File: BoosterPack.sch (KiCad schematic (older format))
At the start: 0 parts

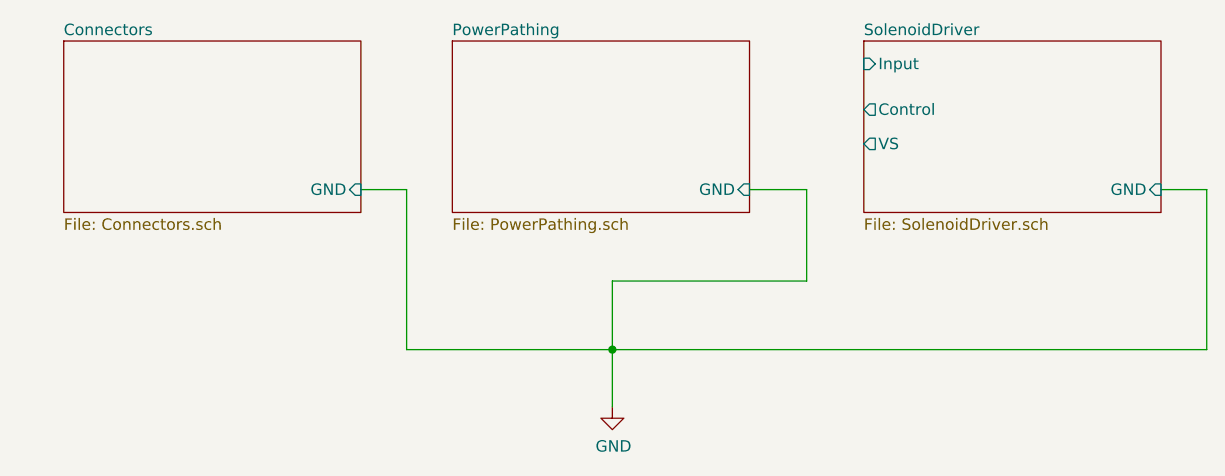
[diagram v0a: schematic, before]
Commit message: Schematic Updates
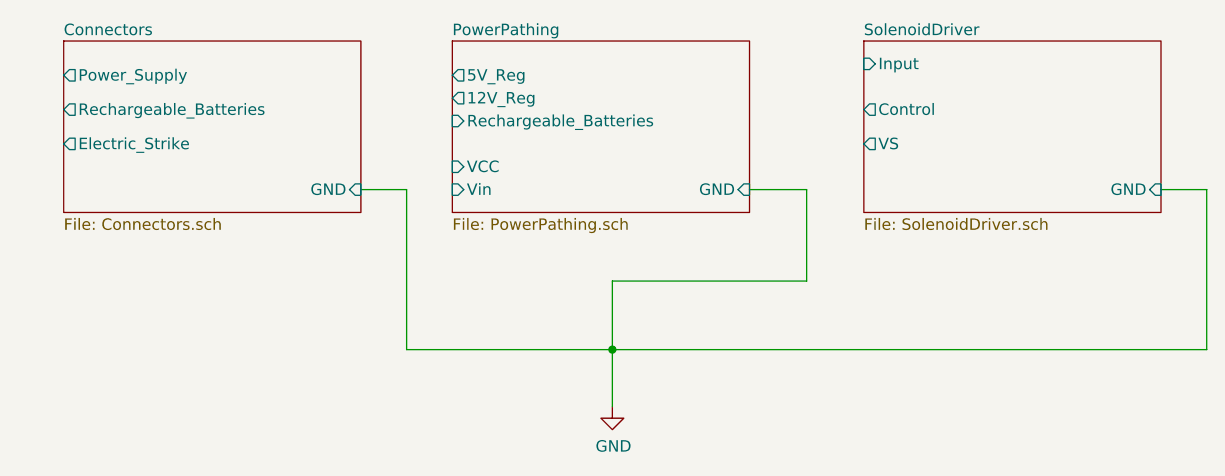
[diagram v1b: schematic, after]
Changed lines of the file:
@@
 F1 "PowerPathing.sch" 50
 F2 "GND" I R 4850 3300 50
+F3 "Vin" I L 3550 3300 50
+F4 "VCC" I L 3550 3200 50
+F5 "Rechargeable_Batteries" I L 3550 3000 50
+F6 "5V_Reg" O L 3550 2800 50
+F7 "12V_Reg" O L 3550 2900 50
 $EndSheet
 $Sheet
@@
 F1 "Connectors.sch" 50
 F2 "GND" I R 3150 3300 50
+F3 "Power_Supply" O L 1850 2800 50
+F4 "Rechargeable_Batteries" O L 1850 2950 50
+F5 "Electric_Strike" O L 1850 3100 50
 $EndSheet
 $Comp

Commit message: Schematic Updates, still need component values for driver circuit and keypad connector EDA
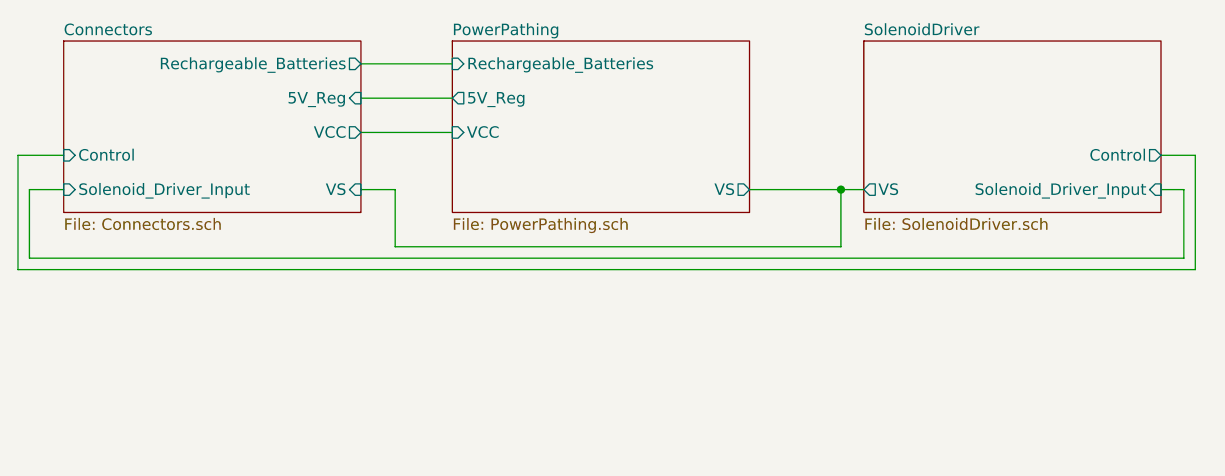
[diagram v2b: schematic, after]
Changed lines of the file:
@@
 F0 "PowerPathing" 50
 F1 "PowerPathing.sch" 50
-F2 "GND" I R 4850 3300 50
-F3 "Vin" I L 3550 3300 50
-F4 "VCC" I L 3550 3200 50
-F5 "Rechargeable_Batteries" I L 3550 3000 50
-F6 "5V_Reg" O L 3550 2800 50
-F7 "12V_Reg" O L 3550 2900 50
+F2 "VCC" I L 3550 3050 50
+F3 "Rechargeable_Batteries" I L 3550 2750 50
+F4 "5V_Reg" O L 3550 2900 50
+F5 "VS" O R 4850 3300 50
+$EndSheet
+$Sheet
+S 1850 2650 1300 750
+U 61536750
+F0 "Connectors" 50
+F1 "Connectors.sch" 50
+F2 "Rechargeable_Batteries" O R 3150 2750 50
+F3 "5V_Reg" I R 3150 2900 50
+F4 "Solenoid_Driver_Input" I L 1850 3300 50
+F5 "VCC" O R 3150 3050 50
+F6 "VS" I R 3150 3300 50
+F7 "Control" I L 1850 3150 50
 $EndSheet
 $Sheet
@@
 F0 "SolenoidDriver" 50
 F1 "SolenoidDriver.sch" 50
-F2 "GND" I R 6650 3300 50
-F3 "Control" O L 5350 2950 50
-F4 "VS" O L 5350 3100 50
-F5 "Input" I L 5350 2750 50
+F2 "Control" O R 6650 3150 50
+F3 "VS" O L 5350 3300 50
+F4 "Solenoid_Driver_Input" I R 6650 3300 50
 $EndSheet
-$Sheet
-S 1850 2650 1300 750
-U 61536750
-F0 "Connectors" 50
-F1 "Connectors.sch" 50
-F2 "GND" I R 3150 3300 50
-F3 "Power_Supply" O L 1850 2800 50
-F4 "Rechargeable_Batteries" O L 1850 2950 50
-F5 "Electric_Strike" O L 1850 3100 50
-$EndSheet
-$Comp
-L power:GND #PWR?
-U 1 1 615662EA
-P 4250 4250
-F 0 "#PWR?" H 4250 4000 50  0001 C CNN
-F 1 "GND" H 4255 4077 50  0000 C CNN
-F 2 "" H 4250 4250 50  0001 C CNN
-F 3 "" H 4250 4250 50  0001 C CNN
-	1    4250 4250
-	1    0    0    -1
-$EndComp
 Wire Wire Line
-	4250 4250 4250 4000
+	3150 2750 3550 2750
 Wire Wire Line
-	4250 4000 3350 4000
+	3150 2900 3550 2900
 Wire Wire Line
-	3350 4000 3350 3300
+	3150 3050 3550 3050
 Wire Wire Line
-	3350 3300 3150 3300
+	4850 3300 5250 3300
 Wire Wire Line
-	5100 3300 4850 3300
-Connection ~ 4250 4000
+	5250 3300 5250 3550
 Wire Wire Line
-	6850 4000 6850 3300
+	5250 3550 3300 3550
 Wire Wire Line
-	6850 3300 6650 3300
+	3300 3550 3300 3300
 Wire Wire Line
-	4250 4000 6850 4000
+	3300 3300 3150 3300
+Connection ~ 5250 3300
 Wire Wire Line
-	4250 4000 4250 3700
+	5250 3300 5350 3300
 Wire Wire Line
-	4250 3700 5100 3700
+	6650 3300 6750 3300
 Wire Wire Line
-	5100 3700 5100 3300
+	6750 3300 6750 3600
+Wire Wire Line
+	6750 3600 1700 3600
+Wire Wire Line
+	1700 3600 1700 3300
+Wire Wire Line
+	1700 3300 1850 3300
+Wire Wire Line
+	1850 3150 1650 3150
+Wire Wire Line
+	1650 3150 1650 3650
+Wire Wire Line
+	1650 3650 6800 3650
+Wire Wire Line
+	6800 3650 6800 3150
+Wire Wire Line
+	6800 3150 6650 3150
 $EndSCHEMATC
